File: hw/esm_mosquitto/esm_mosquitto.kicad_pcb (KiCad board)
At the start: 2 copper layers, 12 parts, among them J1 Conn_01x04_Male, J2 Barrel_Jack, U1 ESP-01v090, U2 DHT11, U3 BSS138_4ch, U4 LM317_TO-220

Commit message: Компоновка завершена
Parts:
- added C1: 1u, Capacitor_THT:C_Disc_D3.8mm_W2.6mm_P2.50mm, F.Cu at (180.3, 76.2)
- added C2: 220u, Capacitor_THT:CP_Radial_D5.0mm_P2.50mm, F.Cu at (185.4, 76.2)
- added D1: LED_B_wifi, LED_THT:LED_D5.0mm_Clear, F.Cu at (175.3, 55.9)
- added D2: LED_R_mqtt, LED_THT:LED_D5.0mm_Clear, F.Cu at (160.0, 55.9)
- added D3: LED_Y_soil, LED_THT:LED_D5.0mm_Clear, F.Cu at (167.6, 55.9)
- added R10: 470, Resistor_THT:R_Axial_DIN0207_L6.3mm_D2.5mm_P7.62mm_Horizontal, F.Cu at (162.6, 62.2)
- added R2: R_Photo, Connector_PinHeader_2.54mm:PinHeader_1x02_P2.54mm_Vertical, F.Cu at (128.9, 73.7)
- added R4: R_Photo, Connector_PinHeader_2.54mm:PinHeader_1x02_P2.54mm_Vertical, F.Cu at (134.6, 73.7)
- added R8: 470, Resistor_THT:R_Axial_DIN0207_L6.3mm_D2.5mm_P7.62mm_Horizontal, F.Cu at (165.1, 62.2)
- added R9: 470, Resistor_THT:R_Axial_DIN0207_L6.3mm_D2.5mm_P7.62mm_Horizontal, F.Cu at (160.0, 62.2)
- J1: value Conn_01x04_Male -> Conn_01x04_Male_Soil_Sensor; footprint Connector_PinHeader_2.54mm:PinHeader_1x04_P2.54mm_Horizontal -> Connector_PinHeader_2.54mm:PinHeader_1x04_P2.54mm_Vertical
- R1, R3: value R -> 1k
- R5: value R -> 10k
- moved J1 55.0 mm to (134.6, 58.4)
- moved R7 29.7 mm to (177.8, 66.0)
- moved U4 29.7 mm to (184.2, 71.1), turned to 180 degrees
- moved R6 29.6 mm to (174.0, 72.4), turned to 90 degrees
- moved R5 26.1 mm to (167.6, 73.7), turned to 180 degrees
- moved J2 22.9 mm to (132.1, 96.5)
- moved U2 19.9 mm to (168.8, 78.7), turned to -90 degrees
- moved R3 15.7 mm to (134.6, 83.8)
- moved R1 15.5 mm to (128.9, 83.8)
- moved U1 14.4 mm to (180.3, 94.0), turned to 180 degrees
- moved A1 12.7 mm to (154.9, 95.2)
- moved U3 12.7 mm to (165.1, 91.4)
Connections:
- A1 pad 19: unconnected-(A1-Pad19) -> A0
- A1 pad 5: unconnected-(A1-Pad5) -> Net-(A1-Pad5)
- A1 pad 6: unconnected-(A1-Pad6) -> Net-(A1-Pad6)
- A1 pad 7: unconnected-(A1-Pad7) -> Net-(A1-Pad7)
- J1 pad 1: unconnected-(J1-Pad1) -> +5V
- J1 pad 2: unconnected-(J1-Pad2) -> GND
- J1 pad 4: unconnected-(J1-Pad4) -> A0

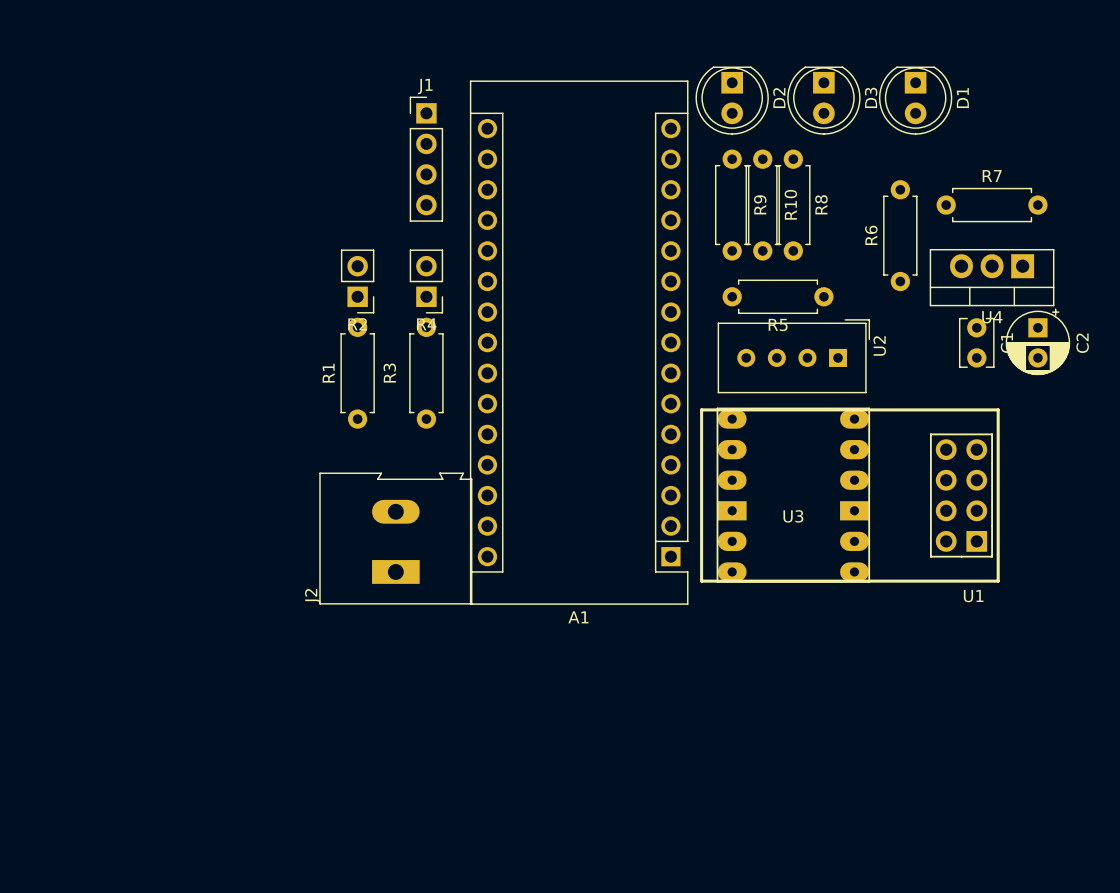
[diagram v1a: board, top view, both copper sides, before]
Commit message: Собрано устройство на паечной макетной плате. Исправлены ошибки при монтаже, проверены напряжения питания. Изменена схема формирования напряжения 3.3 В, переназначены выводы для светодиодов и датчика DHT 22
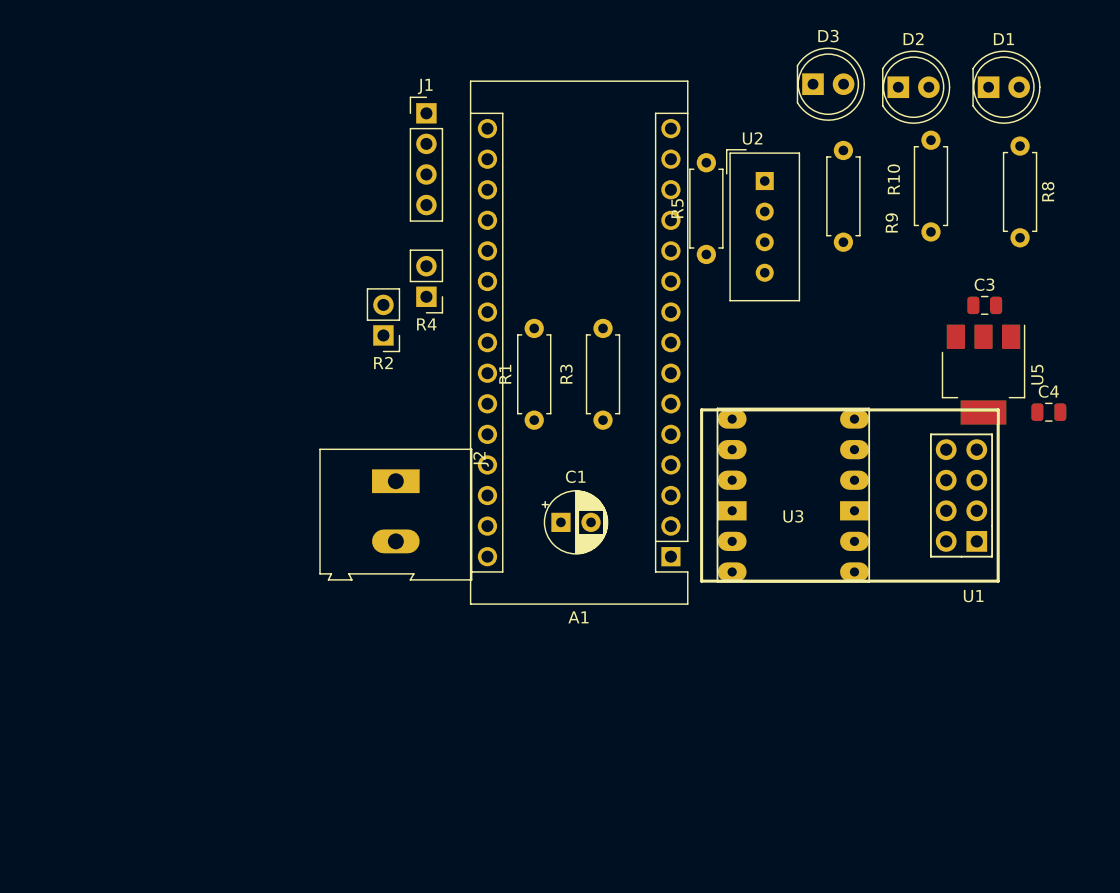
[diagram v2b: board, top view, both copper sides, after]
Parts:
- removed C2: 220u, Capacitor_THT:CP_Radial_D5.0mm_P2.50mm
- removed R6: 200, Resistor_THT:R_Axial_DIN0207_L6.3mm_D2.5mm_P7.62mm_Horizontal
- removed R7: 330, Resistor_THT:R_Axial_DIN0207_L6.3mm_D2.5mm_P7.62mm_Horizontal
- removed U4: LM317_TO-220, Package_TO_SOT_THT:TO-220-3_Vertical
- added C3: 10u, Capacitor_SMD:C_0805_2012Metric, F.Cu at (181.0, 74.4)
- added C4: 22u, Capacitor_SMD:C_0805_2012Metric, F.Cu at (186.3, 83.2)
- added U5: AMS1117-3.3, Package_TO_SOT_SMD:SOT-223-3_TabPin2, F.Cu at (180.9, 80.1)
- C1: value 1u -> 220u; footprint Capacitor_THT:C_Disc_D3.8mm_W2.6mm_P2.50mm -> Capacitor_THT:CP_Radial_D5.0mm_P2.50mm
- D1: value LED_B_wifi -> LED_G_wifi
- D2: value LED_R_mqtt -> LED_Y_soil
- D3: value LED_Y_soil -> LED_R_mqtt
- moved C1 38.1 mm to (145.8, 92.4), turned to 0 degrees
- moved R8 18.9 mm to (183.9, 61.1)
- moved R9 16.6 mm to (176.5, 60.7)
- moved U2 15.9 mm to (162.7, 64.0), turned to 0 degrees
- moved R1 14.7 mm to (143.6, 83.9)
- moved R3 14.7 mm to (149.3, 83.9)
- moved D2 13.8 mm to (173.8, 56.2), turned to 0 degrees
- moved R5 10.4 mm to (157.9, 70.1), turned to 90 degrees
- moved J2 7.54 mm to (132.1, 89.0), turned to -90 degrees
- moved R10 6.74 mm to (169.3, 61.5)
- moved D1 6.07 mm to (181.3, 56.2), turned to 0 degrees
- moved R2 3.86 mm to (131.1, 76.9)
- moved D3 0.91 mm to (166.7, 56.0), turned to 0 degrees
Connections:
- A1 pad 10: unconnected-(A1-Pad10) -> Net-(A1-Pad10)
- A1 pad 11: unconnected-(A1-Pad11) -> Net-(A1-Pad11)
- A1 pad 14: unconnected-(A1-Pad14) -> DHT_OUT
- A1 pad 30: VIN -> unconnected-(A1-Pad30)
- A1 pad 5: Net-(A1-Pad5) -> unconnected-(A1-Pad5)
- A1 pad 6: Net-(A1-Pad6) -> unconnected-(A1-Pad6)
- A1 pad 7: Net-(A1-Pad7) -> unconnected-(A1-Pad7)
- A1 pad 9: DHT_OUT -> Net-(A1-Pad9)
- C1 pad 1: +3V3 -> +5V
- J2 pad 1: VIN -> +5V
- R10 pad 2: Net-(A1-Pad7) -> Net-(A1-Pad11)
- R8 pad 2: Net-(A1-Pad5) -> Net-(A1-Pad9)
- R9 pad 2: Net-(A1-Pad6) -> Net-(A1-Pad10)

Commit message: - Исправлена ошибка в подключении ESP 01: вывод EN подтянут к питанию - Допаяны последние провода - Устройство собрано в корпус
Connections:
- U1 pad 3: unconnected-(U1-Pad3) -> +3V3
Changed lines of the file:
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@@
   (net 19 "unconnected-(U2-Pad3)")
   (net 20 "GND")
-  (net 21 "unconnected-(U1-Pad3)")
+  (net 21 "Net-(D1-Pad2)")
   (net 22 "unconnected-(U1-Pad4)")
   (net 23 "unconnected-(U1-Pad5)")
@@
   (net 41 "Net-(A1-Pad10)")
   (net 42 "Net-(A1-Pad11)")
-  (net 43 "Net-(R8-Pad1)")
-  (net 44 "Net-(R9-Pad1)")
-  (net 45 "Net-(R10-Pad1)")
+  (net 43 "Net-(D2-Pad2)")
+  (net 44 "Net-(D3-Pad2)")
   (footprint "Connector_PinHeader_2.54mm:PinHeader_1x04_P2.54mm_Vertical" (layer "F.Cu")
     (at 134.62 58.42)
@@
     (fp_line (start 6.96 -1.25) (end 0.66 -1.25) (layer "F.Fab") (width 0.1))
     (pad "1" thru_hole circle (at 0 0 270) (size 1.6 1.6) (drill 0.8) (layers *.Cu *.Mask)
-      (net 45 "Net-(R10-Pad1)") (pintype "passive"))
+      (net 44 "Net-(D3-Pad2)") (pintype "passive"))
     (pad "2" thru_hole oval (at 7.62 0 270) (size 1.6 1.6) (drill 0.8) (layers *.Cu *.Mask)
       (net 42 "Net-(A1-Pad11)") (pintype "passive"))
@@
     (fp_line (start 0.66 1.25) (end 6.96 1.25) (layer "F.Fab") (width 0.1))
     (pad "1" thru_hole circle (at 0 0 270) (size 1.6 1.6) (drill 0.8) (layers *.Cu *.Mask)
-      (net 44 "Net-(R9-Pad1)") (pintype "passive"))
+      (net 43 "Net-(D2-Pad2)") (pintype "passive"))
     (pad "2" thru_hole oval (at 7.62 0 270) (size 1.6 1.6) (drill 0.8) (layers *.Cu *.Mask)
       (net 41 "Net-(A1-Pad10)") (pintype "passive"))
@@
       (net 20 "GND") (pinfunction "K") (pintype "passive"))
     (pad "2" thru_hole circle (at 2.54 0) (size 1.8 1.8) (drill 0.9) (layers *.Cu *.Mask)
-      (net 45 "Net-(R10-Pad1)") (pinfunction "A") (pintype "passive"))
+      (net 44 "Net-(D3-Pad2)") (pinfunction "A") (pintype "passive"))
     (model "${KICAD6_3DMODEL_DIR}/LED_THT.3dshapes/LED_D5.0mm_Clear.wrl"
       (offset (xyz 0 0 0))
@@
       (net 20 "GND") (pinfunction "K") (pintype "passive"))
     (pad "2" thru_hole circle (at 2.54 0) (size 1.8 1.8) (drill 0.9) (layers *.Cu *.Mask)
-      (net 43 "Net-(R8-Pad1)") (pinfunction "A") (pintype "passive"))
+      (net 21 "Net-(D1-Pad2)") (pinfunction "A") (pintype "passive"))
     (model "${KICAD6_3DMODEL_DIR}/LED_THT.3dshapes/LED_D5.0mm_Clear.wrl"
       (offset (xyz 0 0 0))
@@
       (net 20 "GND") (pinfunction "K") (pintype "passive"))
     (pad "2" thru_hole circle (at 2.54 0) (size 1.8 1.8) (drill 0.9) (layers *.Cu *.Mask)
-      (net 44 "Net-(R9-Pad1)") (pinfunction "A") (pintype "passive"))
+      (net 43 "Net-(D2-Pad2)") (pinfunction "A") (pintype "passive"))
     (model "${KICAD6_3DMODEL_DIR}/LED_THT.3dshapes/LED_D5.0mm_Clear.wrl"
       (offset (xyz 0 0 0))
@@
       (net 20 "GND") (pinfunction "GND") (pintype "power_in"))
     (pad "3" thru_hole oval locked (at 0 2.54 180) (size 1.7272 1.7272) (drill 1.016) (layers *.Cu *.Mask "F.SilkS")
-      (net 21 "unconnected-(U1-Pad3)") (pinfunction "CH_PD") (pintype "input"))
+      (net 25 "+3V3") (pinfunction "CH_PD") (pintype "input"))
     (pad "4" thru_hole oval locked (at 2.54 2.54 180) (size 1.7272 1.7272) (drill 1.016) (layers *.Cu *.Mask "F.SilkS")
       (net 22 "unconnected-(U1-Pad4)") (pinfunction "GPIO2") (pintype "tri_state"))
@@
     (fp_line (start 0.66 -1.25) (end 0.66 1.25) (layer "F.Fab") (width 0.1))
     (pad "1" thru_hole circle (at 0 0 270) (size 1.6 1.6) (drill 0.8) (layers *.Cu *.Mask)
-      (net 43 "Net-(R8-Pad1)") (pintype "passive"))
+      (net 21 "Net-(D1-Pad2)") (pintype "passive"))
     (pad "2" thru_hole oval (at 7.62 0 270) (size 1.6 1.6) (drill 0.8) (layers *.Cu *.Mask)
       (net 40 "Net-(A1-Pad9)") (pintype "passive"))

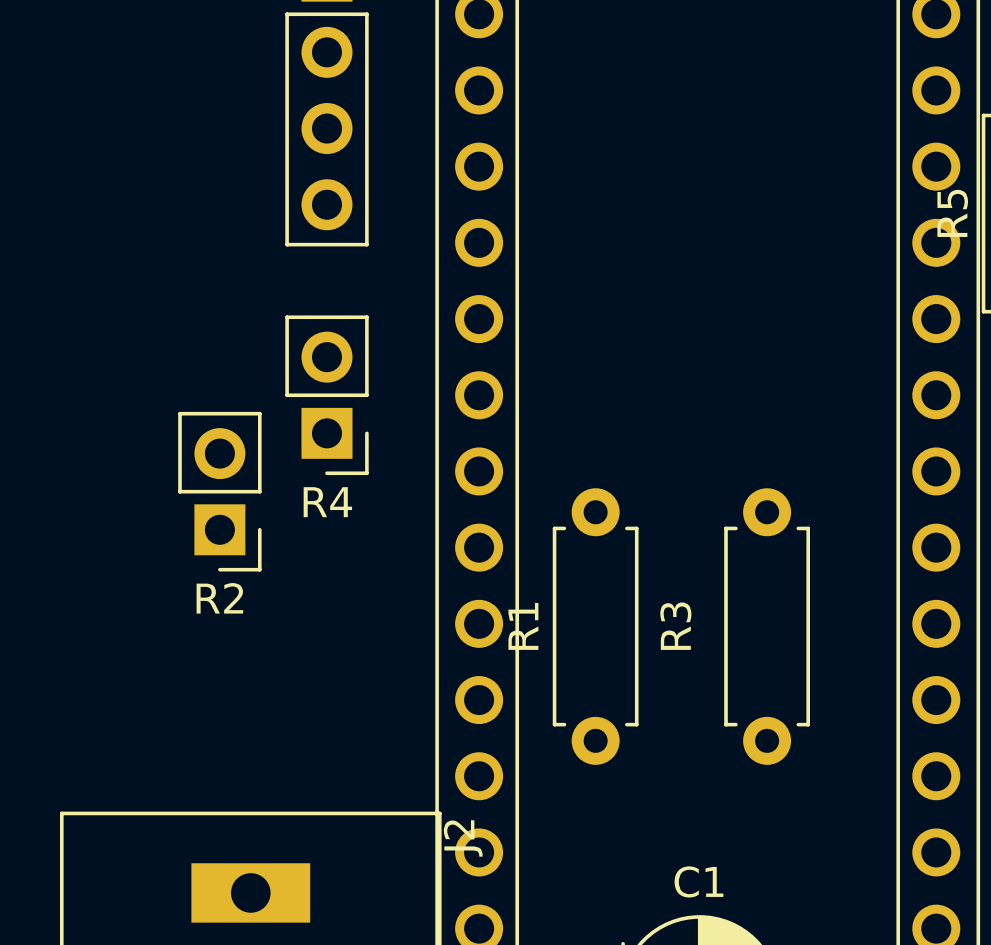
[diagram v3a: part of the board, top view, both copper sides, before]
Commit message: - Исправлено подключение фоторезисторов: фоторезистор и резистор 1к поменяны местами - Допаян длинный провод для вилки датчика влажности почвы - Устройство проверено, работает как ожидается
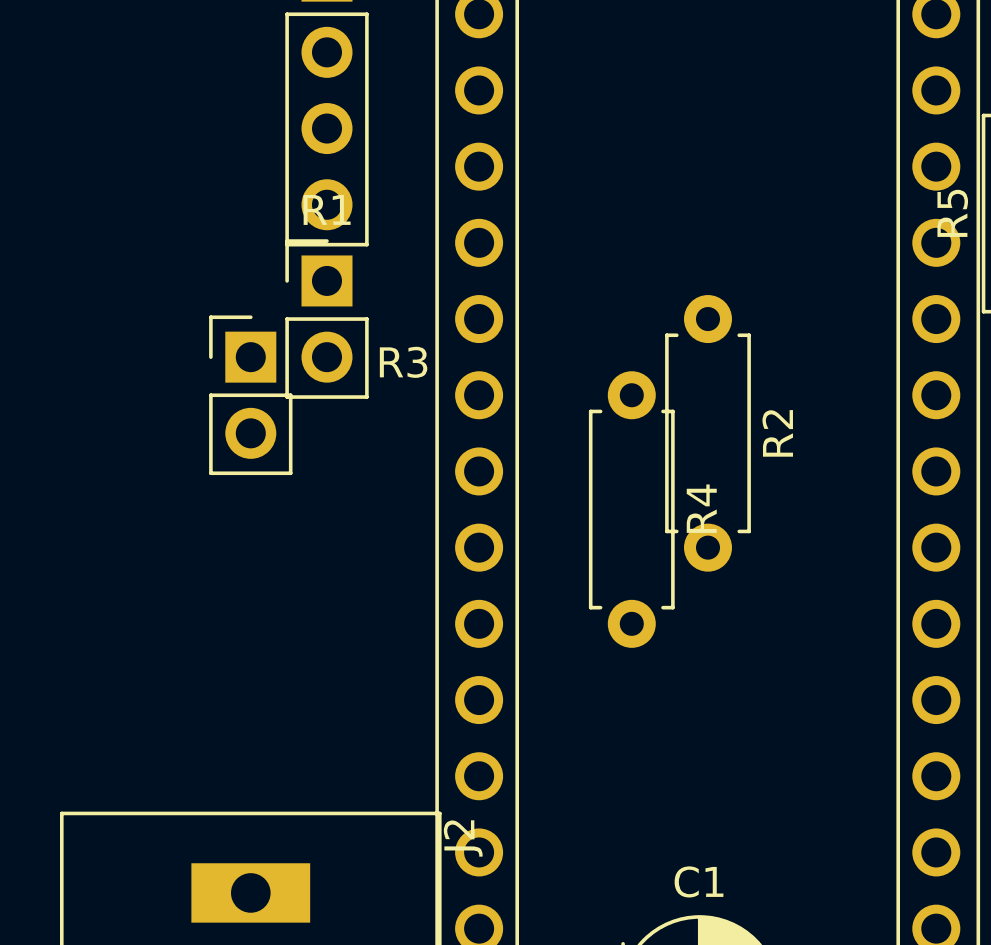
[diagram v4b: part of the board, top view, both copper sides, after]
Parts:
- R1, R3: value 1k -> R_Photo; footprint Resistor_THT:R_Axial_DIN0207_L6.3mm_D2.5mm_P7.62mm_Horizontal -> Connector_PinHeader_2.54mm:PinHeader_1x02_P2.54mm_Vertical
- R2, R4: value R_Photo -> 1k; footprint Connector_PinHeader_2.54mm:PinHeader_1x02_P2.54mm_Vertical -> Resistor_THT:R_Axial_DIN0207_L6.3mm_D2.5mm_P7.62mm_Horizontal
- moved R3 21.4 mm to (132.1, 71.1), turned to 0 degrees
- moved R1 17.8 mm to (134.6, 68.6), turned to 0 degrees
- moved R2 17.7 mm to (147.3, 69.8), turned to -90 degrees
- moved R4 10.2 mm to (144.8, 72.4), turned to -90 degrees
